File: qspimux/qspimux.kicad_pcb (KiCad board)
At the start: 2 copper layers, 24.8 x 13.8 mm, 9 parts, among them J101 Conn_02x05_Odd_Even, J102 Conn_02x04_Odd_Even, J103 Conn_02x04_Odd_Even, Q101 PMV50XP, Q102 PMV50XP, U101 TS3A27518ERTWR

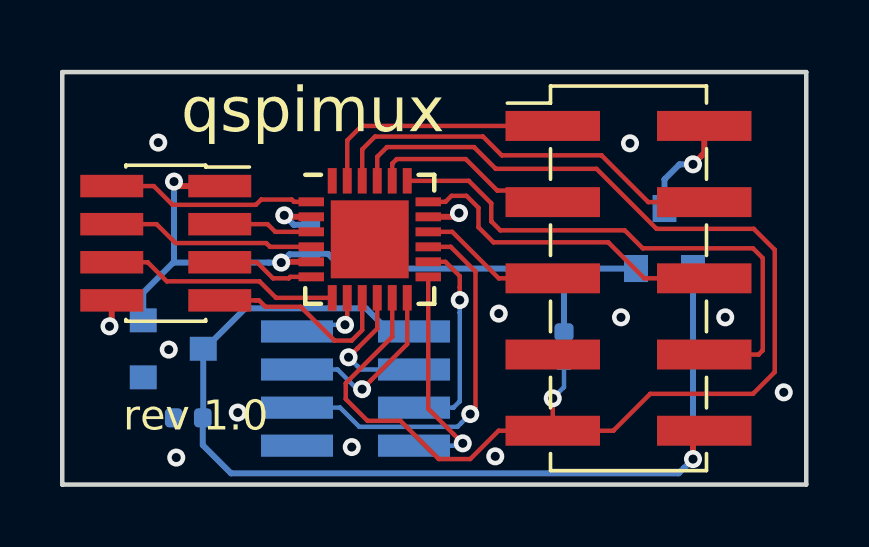
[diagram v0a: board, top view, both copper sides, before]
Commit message: fix power supply circuitry
The old version was lacking reverse current protection on Q101.
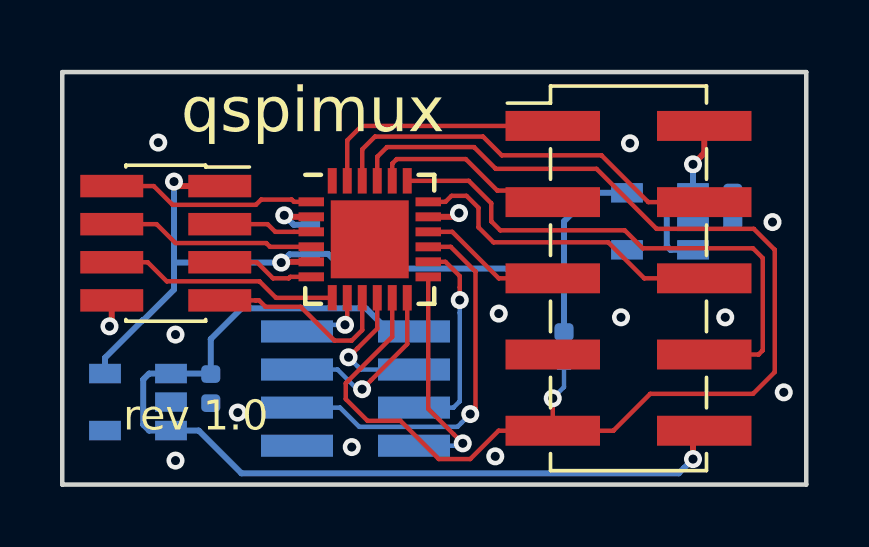
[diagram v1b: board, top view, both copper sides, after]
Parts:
- removed Q101, Q102: PMV50XP, Package_TO_SOT_SMD:SOT-23
- removed R102: 4k7, Resistor_SMD:R_0402_1005Metric
- added C102: 100n, Capacitor_SMD:C_0402_1005Metric, B.Cu at (95.8, 96.8)
- added C103: 100n, Capacitor_SMD:C_0402_1005Metric, B.Cu at (113.2, 90.7)
- added U102: MAX40200AUK, Package_TO_SOT_SMD:SOT-23-5, B.Cu at (93.3, 97.2)
- added U103: MAX40200AUK, Package_TO_SOT_SMD:SOT-23-5, B.Cu at (110.7, 91.2)
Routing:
- net /VCC_FLASH: track 25.5 -> 29.5 mm
- net /VCC_PROG: track 3.57 -> 7.21 mm
- net /VCC_BOARD: track 35.6 -> 33.0 mm
- net GND: vias 14 -> 15

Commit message: move layout-related TODO to layout file
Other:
- board text added: "TODO: fix TS3A27518ERTWR footprint"
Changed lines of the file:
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@@
   (general
     (thickness 1.6)
-    (drawings 7)
+    (drawings 8)
     (tracks 224)
     (zones 0)
@@
     )
   )
+  (gr_text "TODO: fix TS3A27518ERTWR footprint" (at 102.275 83.85) (layer Cmts.User)
+    (effects (font (size 1.5 1.5) (thickness 0.3)))
+  )
   (gr_text "rev 1.0" (at 95.25 97.675) (layer F.SilkS)

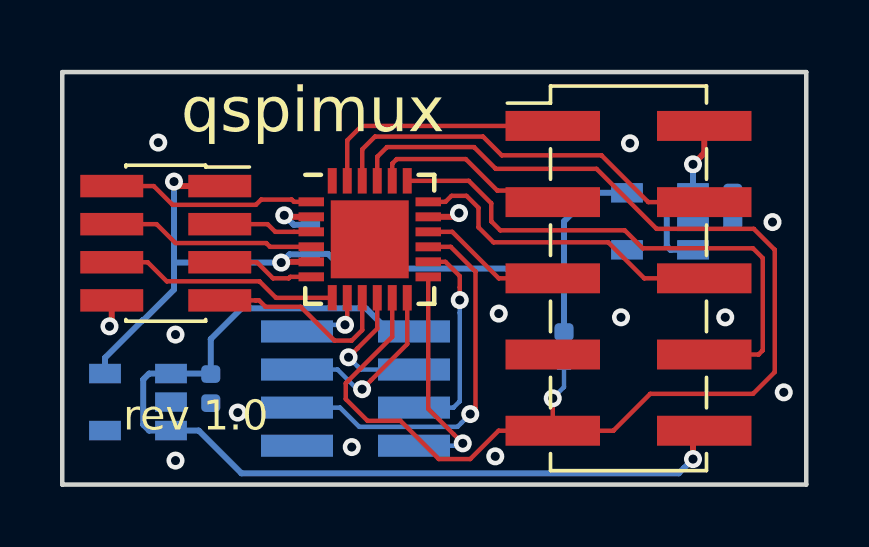
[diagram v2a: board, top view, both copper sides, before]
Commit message: increase trace width
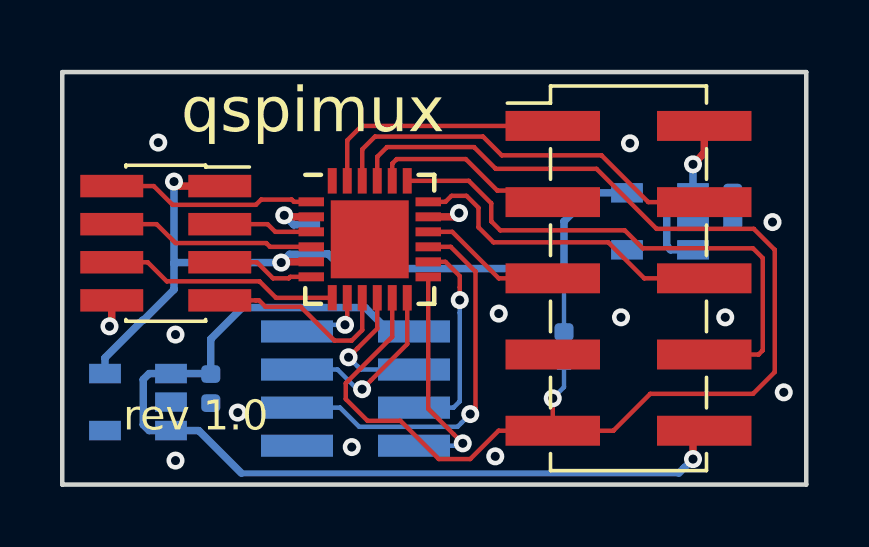
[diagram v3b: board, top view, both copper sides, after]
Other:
- net class power: trace_width 0.2 -> 0.25

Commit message: remove pin 1 markers from wrong position
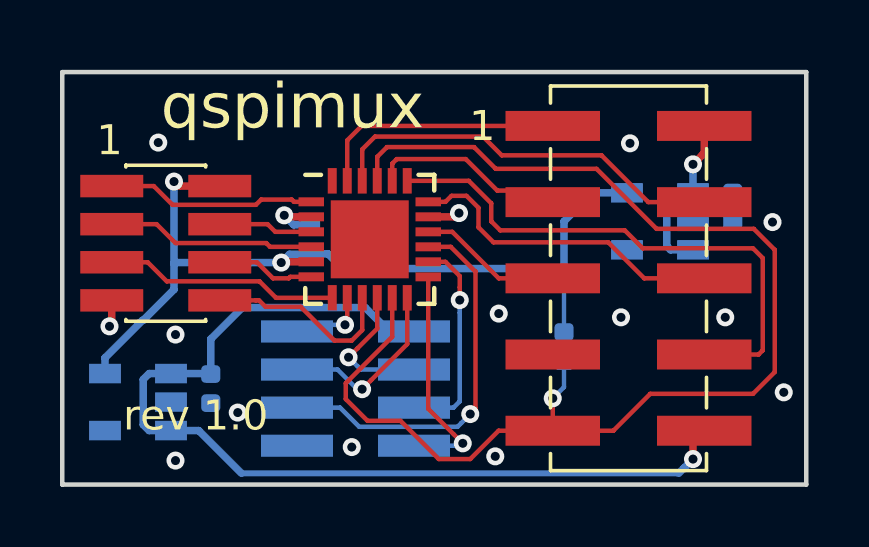
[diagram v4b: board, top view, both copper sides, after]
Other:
- board text added: "1"

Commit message: fix footprint of TS3A27518ERTWR
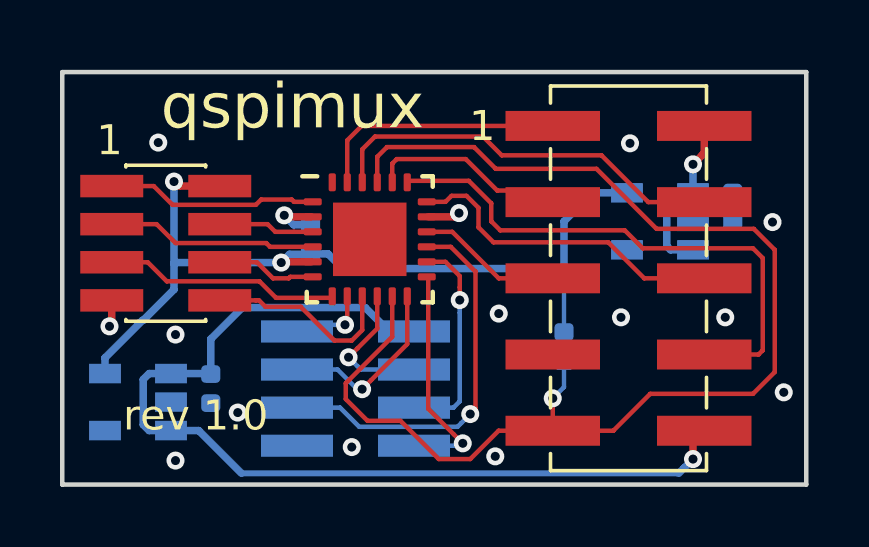
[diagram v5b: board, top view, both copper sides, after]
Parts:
- U101: footprint Package_DFN_QFN:QFN-24-1EP_4x4mm_P0.5mm_EP2.6x2.6mm -> Package_DFN_QFN:QFN-24_1EP_3.9x3.9mm_Pitch0.5mm
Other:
- board text removed: "TODO: fix TS3A27518ERTWR footprint"

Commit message: qspimux: add fiducials
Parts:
- added REF**: Fiducial_0.5mm_Dia_1mm_Outer, Fiducial:Fiducial_0.5mm_Dia_1mm_Outer, F.Cu at (91.8, 87.3)
- added REF**: Fiducial_0.5mm_Dia_1mm_Outer, Fiducial:Fiducial_0.5mm_Dia_1mm_Outer, F.Cu at (114.6, 89.2)
- added REF**: Fiducial_0.5mm_Dia_1mm_Outer, Fiducial:Fiducial_0.5mm_Dia_1mm_Outer, F.Cu at (93.0, 97.5)
- added REF**: Fiducial_0.5mm_Dia_1mm_Outer, Fiducial:Fiducial_0.5mm_Dia_1mm_Outer, B.Cu at (114.6, 89.2)
- added REF**: Fiducial_0.5mm_Dia_1mm_Outer, Fiducial:Fiducial_0.5mm_Dia_1mm_Outer, B.Cu at (114.0, 98.7)
- added REF**: Fiducial_0.5mm_Dia_1mm_Outer, Fiducial:Fiducial_0.5mm_Dia_1mm_Outer, B.Cu at (92.1, 89.6)

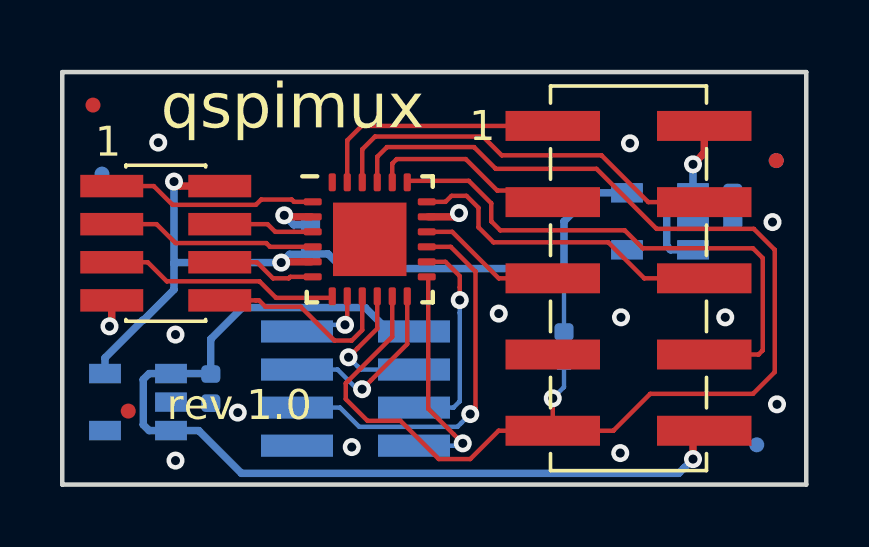
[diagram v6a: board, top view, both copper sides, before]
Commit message: qspimux: fix fiducial pad that was misaligned with its footprint
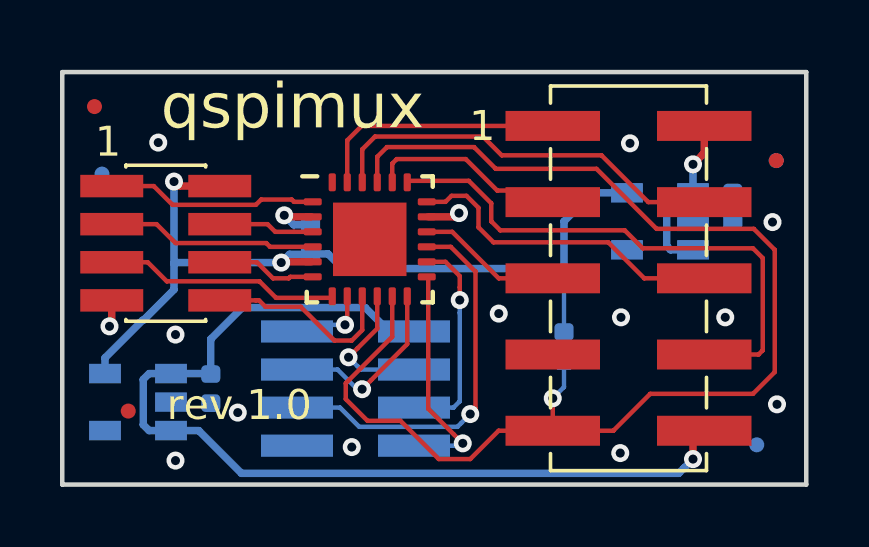
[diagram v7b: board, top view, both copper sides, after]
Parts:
- moved REF** 0.07 mm to (91.9, 87.4)
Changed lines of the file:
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@@
   )
   (module Fiducial:Fiducial_0.5mm_Dia_1mm_Outer (layer F.Cu)
-    (at 91.825 87.325)
+    (at 91.875 87.375)
     (descr "Circular Fiducial, 0.5mm bare copper top; 1mm keepout (Level C)")
     (tags marker)
